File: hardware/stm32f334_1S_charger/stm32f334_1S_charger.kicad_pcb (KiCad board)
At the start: 2 copper layers, 69 parts, among them J1 POWER_IN, J10 Conn_01x01, J11 Conn_01x01, J12 Conn_01x01, J13 Conn_01x01, J14 TP1, J2 Conn_01x05, J3 Conn_01x10, J4 BATTERY, J5 Conn_01x01, J6 Conn_01x01, J7 Conn_01x01, J8 Conn_01x01, J9 Conn_01x01, Q1 BUK9M52-40E, U1 VXO7805-1000, U2 MIC5504-3.3YM5, U3 STM32F334K6Tx, U4 INA190A3, U5 FAN3100TSX

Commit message: v 1.0 board, pre-production
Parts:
- C7, C8, C9, R9, U4: moved to F.Cu
- moved J2 8.14 mm to (23.1, 61.4)
- moved C1 7.70 mm to (23.7, 40.1)
- moved U2 7.50 mm to (22.7, 47.5)
- moved R7 6.51 mm to (40.1, 57.4)
- moved R6 6.51 mm to (37.6, 57.4)
- moved J3 6.50 mm to (37.6, 61.4)
- moved U5 6.04 mm to (37.2, 38.5)
- moved C10 6.00 mm to (26.9, 48.1), turned to 90 degrees
- moved R1 5.92 mm to (20.1, 59.9)
- moved R8 4.06 mm to (38.6, 33.8), turned to 270 degrees
- moved C9 3.21 mm to (86.5, 23.3), turned to 270 degrees
- moved U1 2.10 mm to (20.9, 36.5)
- moved J11 2.01 mm to (32.5, 39.4)
- moved C3 1.80 mm to (26.2, 41.6)
- moved C7 1.35 mm to (33.1, 33.3)
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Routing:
- net GND: track 18.4 -> 42.5 mm, vias 12 -> 26
- net /NRST: track 45.3 -> 36.7 mm
- net Net-(J2-Pad4): track 36.2 -> 28.4 mm
- net JTAG_SWCLK: track 31.3 -> 23.8 mm
- net JTAG_SWDIO: track 33.3 -> 26.2 mm
- net /PB7: track 10.4 -> 16.2 mm
- net /PB6: track 9.72 -> 14.9 mm
- net /PA15: track 14.6 -> 9.53 mm
- net Net-(J13-Pad1): track 7.60 -> 2.82 mm
- net HTRIM_CHA1: track 19.3 -> 15.0 mm
- net ADC1_IN4: track 55.6 -> 59.8 mm
- net +5V: track 59.3 -> 62.6 mm, vias 2 -> 0
- net ADC1_IN2: track 51.1 -> 48.5 mm, vias 1 -> 0
- net /PB5: track 10.0 -> 12.5 mm
- net Net-(C16-Pad1): track 16.9 -> 19.0 mm, vias 2 -> 3
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
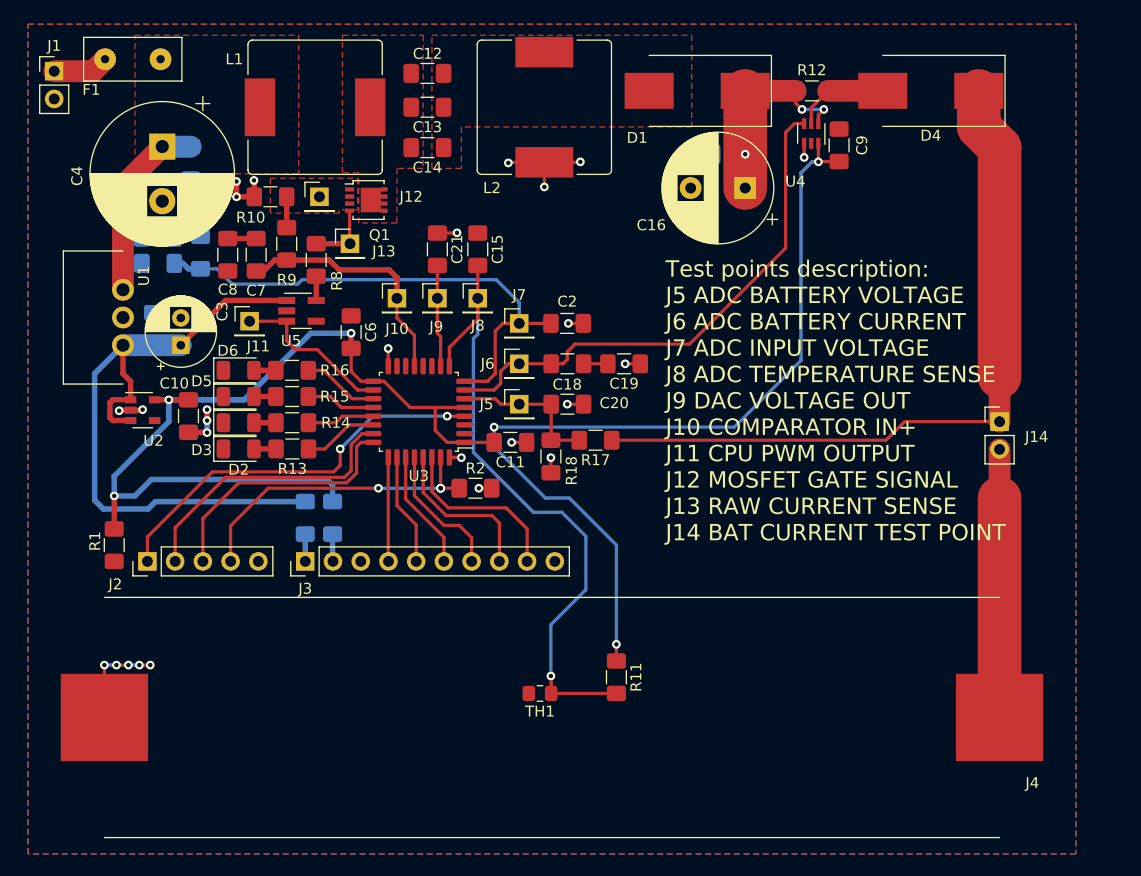
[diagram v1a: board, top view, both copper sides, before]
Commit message: add bom
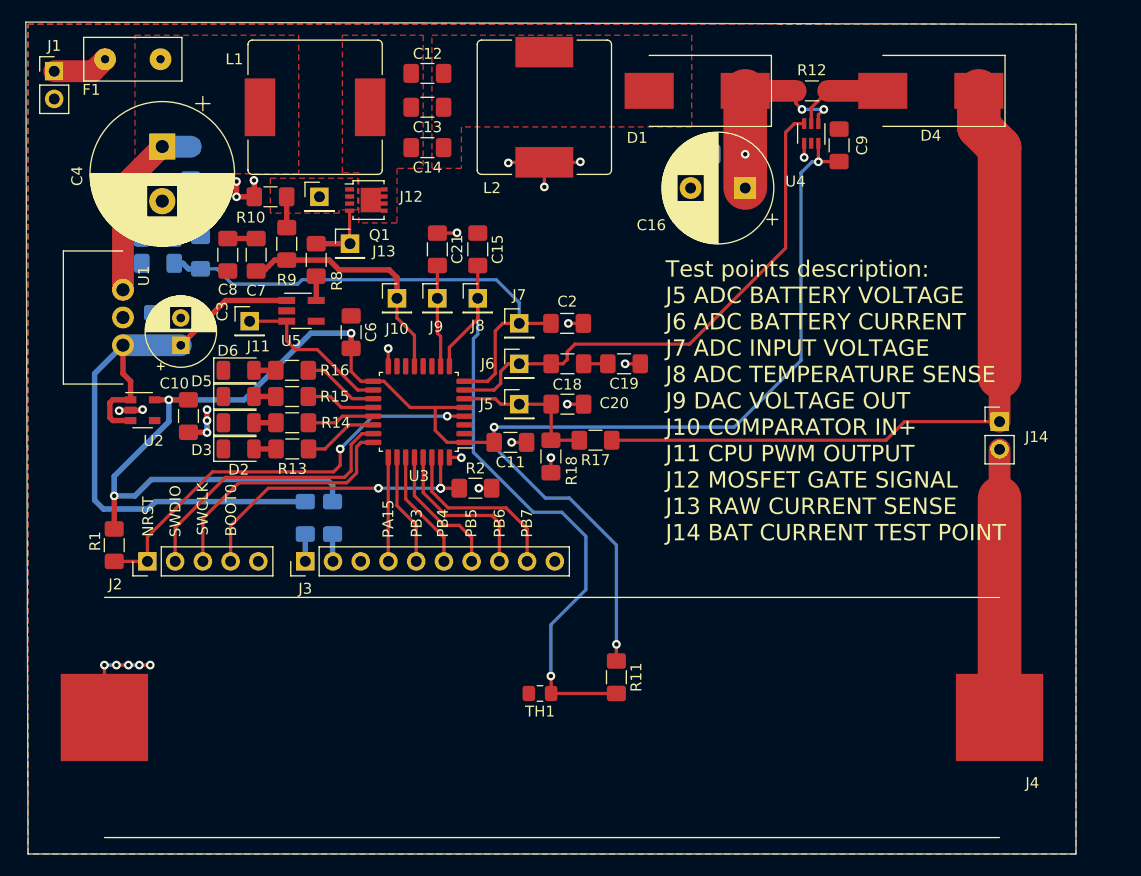
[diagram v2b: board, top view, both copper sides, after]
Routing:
- net /NRST: track 36.7 -> 39.8 mm
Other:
- board outline added: 96.2 x 76.2 mm
- board text added: "BOOT0"
- board text added: "NRST"
- board text added: "PA15"
- board text added: "PB3"
- board text added: "PB4"
- board text added: "PB5"
- board text added: "PB6"
- board text added: "PB7"
- board text added: "SWCLK"
- board text added: "SWDIO"
